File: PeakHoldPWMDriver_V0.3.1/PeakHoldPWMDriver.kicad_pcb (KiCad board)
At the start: 2 copper layers, 100.1 x 50 mm, 120 parts, among them J1 RND 205-00203, J2 RND 205-00205, Q1 2N7002, Q10 2N7002, Q11 2N7002, Q12 2N7002, Q13 TSM2309, Q14 IRLL 024N, Q15 TSM2309, Q16 IRLL 024N, Q17 TSM2309, Q18 TSM2309, Q19 TSM2309, Q2 2N7002, Q20 TSM2309, Q3 2N7002, Q4 2N7002, Q5 TSM2309, Q6 TSM2309, Q7 IRLL 024N, Q8 IRLL 024N, Q9 2N7002, U1 74LS32, U2 LM2901, U3 74LS74, U4 LTC6992, U5 74LS74, U6 LM340, U7 74LS08, U8 74LS08, U9 LM2904

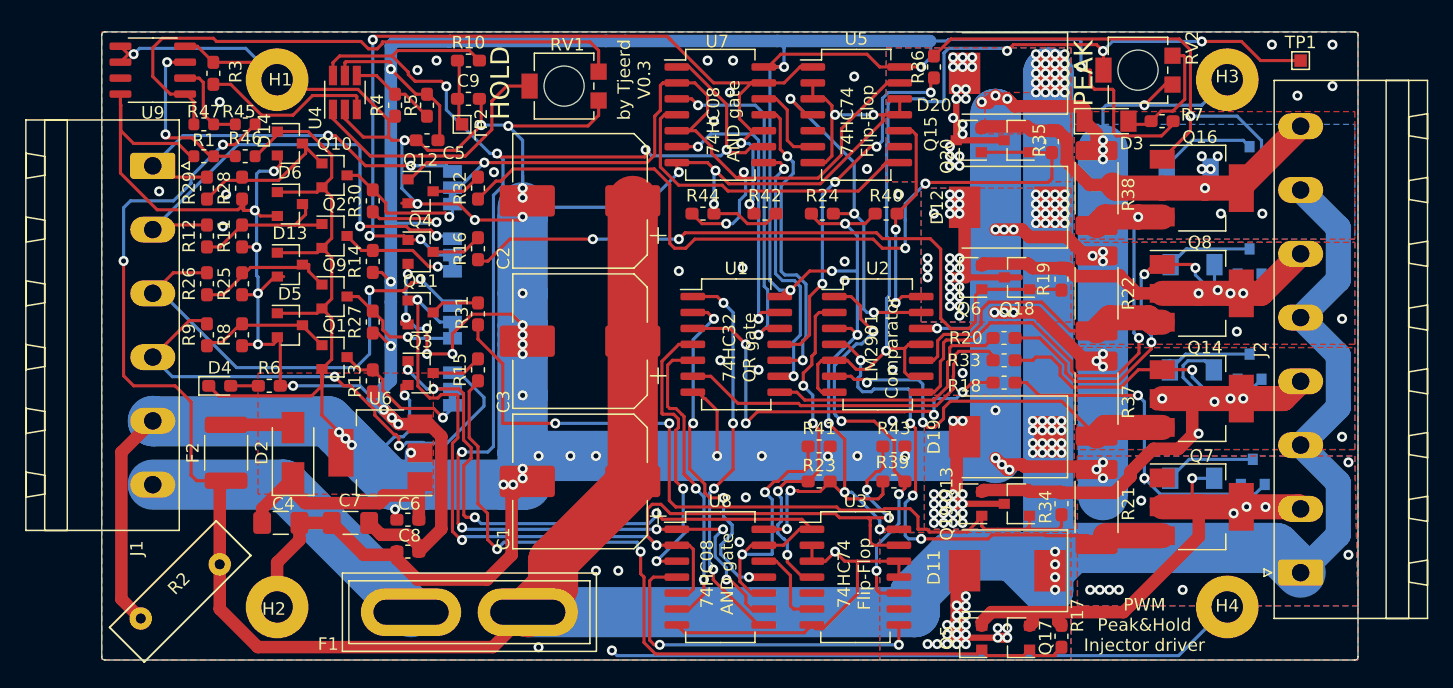
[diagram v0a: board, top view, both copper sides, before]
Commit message: updates values on 0.3 added 0.3.1
Updated resistor values for V0.3
Added V0.3.1 with new battery voltage compensation
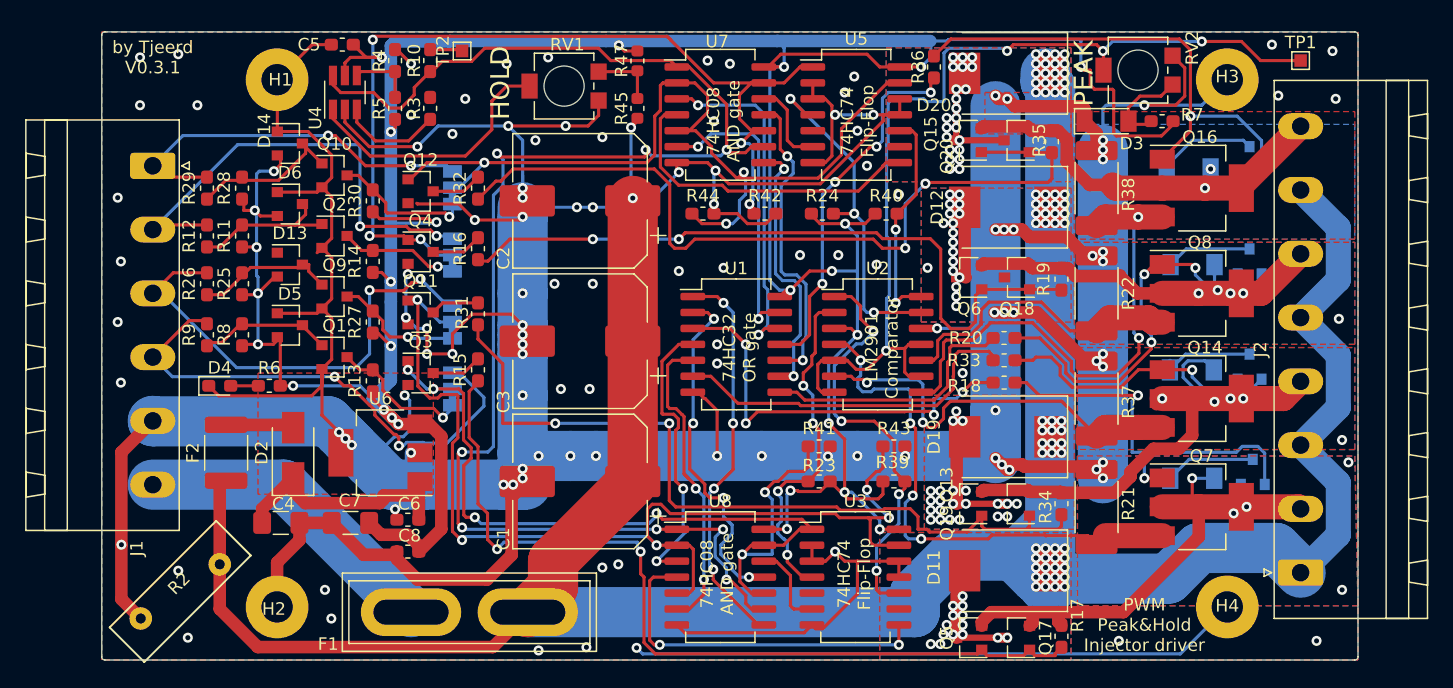
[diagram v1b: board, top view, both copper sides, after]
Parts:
- removed C9: 220nf, Capacitor_SMD:C_0603_1608Metric_Pad1.05x0.95mm_HandSolder
- removed R1: 15k, Resistor_SMD:R_0603_1608Metric
- removed R46: 9.1k, Resistor_SMD:R_0603_1608Metric
- removed U9: LM2904, Package_SO:SO-8_3.9x4.9mm_P1.27mm
- R11, R25, R28, R41, R43, R44, R8: value 1K -> 10K
- R12, R26, R29, R9: value 1K -> 470R
- R4: value 12k -> 100k
- R45: value 91k -> 120k
- R47: value 6.2k -> 33k
- R5: value 100k -> 28k
- moved R47 34.9 mm to (154.4, 68.4), turned to 90 degrees
- moved R45 31.3 mm to (154.4, 72.1), turned to 90 degrees
- moved R3 17.5 mm to (137.9, 72.1)
- moved C5 10.2 mm to (130.9, 67.1)
- moved TP2 5.84 mm to (140.5, 67.6)
- moved R4 3.56 mm to (135.1, 68.3), turned to 270 degrees
- moved R10 3.05 mm to (137.9, 68.3), turned to 270 degrees
- moved R5 2.55 mm to (135.1, 72.1), turned to 90 degrees
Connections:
- R47 pad 2: Net-(R47-Pad2) -> 5V
- RV1 pad 3: Net-(R47-Pad2) -> Net-(R45-Pad2)
- RV2 pad 1: PWR_GND -> Net-(D3-Pad2)
- RV2 pad 3: Net-(D3-Pad2) -> PWR_GND
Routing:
- net PWR_GND: track 617.6 -> 554.4 mm, vias 104 -> 122
- net Net-(R47-Pad2): track 46.7 -> 0.00 mm
- net VBAT: track 261.3 -> 230.4 mm, vias 58 -> 70
- net 5V: track 319.2 -> 288.4 mm, vias 25 -> 27
- net Net-(R1-Pad1): track 13.8 -> 0.00 mm, vias 2 -> 0
- net Net-(R3-Pad1): track 14.2 -> 8.19 mm
- net PWM: track 121.1 -> 126.2 mm, vias 9 -> 8
- net Net-(D12-Pad2): track 9.95 -> 5.63 mm, vias 23 -> 18
- net Net-(D8-Pad2): track 29.3 -> 31.9 mm
- net Net-(R10-Pad1): track 5.09 -> 2.59 mm
- net Net-(D3-Pad2): track 9.71 -> 7.26 mm
- net Net-(R45-Pad2): track 7.26 -> 5.33 mm
- net Net-(R4-Pad2): track 6.93 -> 5.24 mm
- net Net-(D20-Pad2): vias 18 -> 22
- net Net-(D19-Pad2): vias 18 -> 22
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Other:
- board text added: "by Tjeerd V0.3.1"
- board text removed: "by Tjeerd V0.3"

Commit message: Update parts V0.3.1
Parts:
- moved D14 2.10 mm to (126.2, 77.0)
- moved D13 2.09 mm to (126.2, 86.6)
- moved D5 2.09 mm to (126.2, 91.4)
- moved D6 2.09 mm to (126.2, 81.8)
- moved R31 1.89 mm to (141.7, 86.6)
- moved Q3 1.78 mm to (137.2, 91.4)
- moved Q4 1.78 mm to (137.2, 81.8)
- moved R14 1.78 mm to (133.3, 82.5)
- moved Q11 1.78 mm to (137.2, 86.6)
- moved Q12 1.78 mm to (137.2, 77.0)
- moved R15 1.52 mm to (141.7, 91.4)
- moved R16 1.52 mm to (141.7, 81.8)
- moved R27 1.52 mm to (133.3, 87.6)
- moved R30 1.52 mm to (133.3, 78.0)
- moved R32 1.52 mm to (141.7, 77.0)
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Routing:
- net PWR_GND: track 554.4 -> 570.7 mm, vias 122 -> 125
- net INJ2: track 38.1 -> 31.9 mm
- net 5V: track 288.4 -> 292.7 mm, vias 27 -> 26
- net INJ1: track 42.8 -> 39.5 mm
- net Net-(JP3-Pad1): track 10.2 -> 13.3 mm
- net Net-(JP2-Pad1): track 9.93 -> 12.8 mm
- net PWM: track 126.2 -> 128.6 mm
- net Net-(RV1-Pad2): track 21.3 -> 19.0 mm
- net Net-(JP1-Pad1): track 11.9 -> 13.9 mm
- net Net-(D14-Pad3): track 12.4 -> 10.4 mm
- net INJ3: track 38.9 -> 40.5 mm
- net Net-(R39-Pad2): track 34.3 -> 35.8 mm
- net Net-(Q17-Pad1): track 69.0 -> 70.6 mm
- net inv_INJ2: track 85.1 -> 86.6 mm, vias 5 -> 6
- net Net-(D6-Pad3): track 12.0 -> 10.6 mm
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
